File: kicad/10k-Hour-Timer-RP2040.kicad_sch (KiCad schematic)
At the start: 9 parts, among them J1 USB_C_Receptacle_USB2.0_16P, J2 JST_SH_SM03B, U1 USBLC6-2SC6

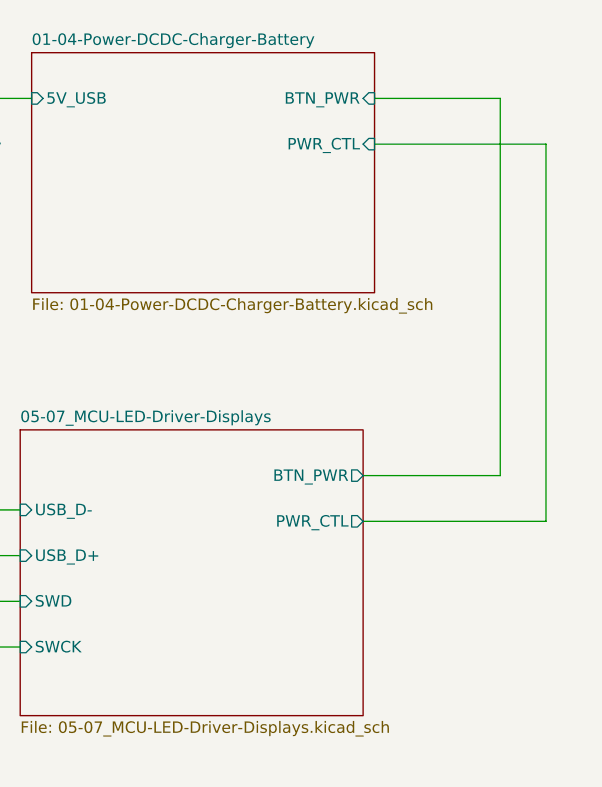
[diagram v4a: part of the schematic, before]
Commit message: rp2040 chip start
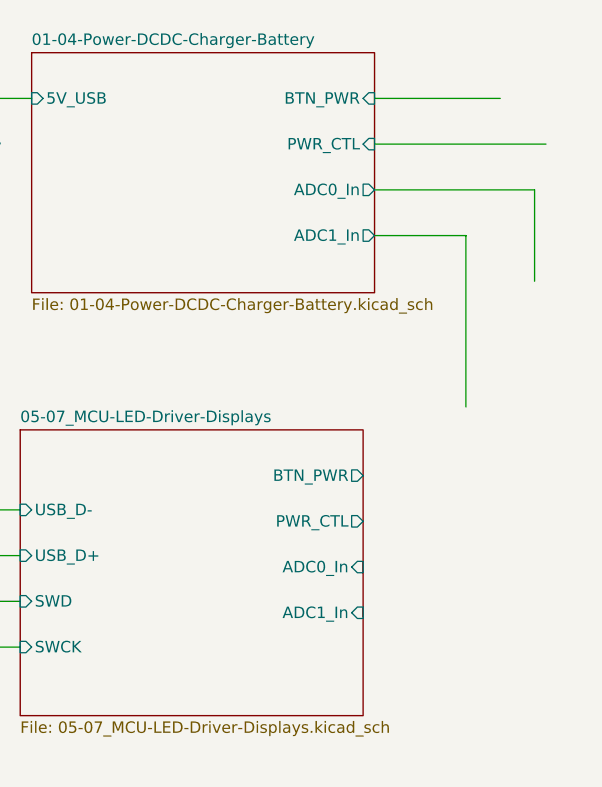
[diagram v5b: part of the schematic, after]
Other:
- sheet 01-04-Power-DCDC-Charger-Battery ports: added ADC0_In, ADC1_In; removed none
- sheet 05-07_MCU-LED-Driver-Displays ports: added ADC0_In, ADC1_In; removed none
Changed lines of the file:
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@@
-	(wire
-		(pts
-			(xy 186.69 99.06) (xy 186.69 57.15)
-		)
-		(stroke
-			(width 0)
-			(type default)
-		)
-	)
-	(wire
-		(pts
-			(xy 191.77 104.14) (xy 171.45 104.14)
-		)
-		(stroke
-			(width 0)
-			(type default)
-		)
-	)
 	(wire
 		(pts
@@
 	(wire
 		(pts
+			(xy 172.72 67.31) (xy 190.5 67.31)
+		)
+		(stroke
+			(width 0)
+			(type default)
+		)
+	)
+	(wire
+		(pts
 			(xy 57.15 123.19) (xy 60.96 123.19)
 		)
@@
 	(wire
 		(pts
-			(xy 191.77 62.23) (xy 191.77 104.14)
-		)
-		(stroke
-			(width 0)
-			(type default)
-		)
-	)
-	(wire
-		(pts
 			(xy 102.87 81.28) (xy 102.87 83.82)
 		)
@@
 	(wire
 		(pts
-			(xy 171.45 99.06) (xy 186.69 99.06)
+			(xy 172.72 72.39) (xy 182.88 72.39)
 		)
 		(stroke
@@
 	(wire
 		(pts
+			(xy 182.88 72.39) (xy 182.88 91.44)
+		)
+		(stroke
+			(width 0)
+			(type default)
+		)
+	)
+	(wire
+		(pts
 			(xy 57.15 120.65) (xy 78.74 120.65)
 		)
@@
 		(pts
 			(xy 73.66 73.66) (xy 73.66 72.39)
+		)
+		(stroke
+			(width 0)
+			(type default)
+		)
+	)
+	(wire
+		(pts
+			(xy 190.5 67.31) (xy 190.5 77.47)
 		)
 		(stroke
@@
 			)
 		)
+		(pin "ADC0_In" input
+			(at 171.45 109.22 0)
+			(effects
+				(font
+					(size 1.27 1.27)
+				)
+				(justify right)
+			)
+		)
+		(pin "ADC1_In" input
+			(at 171.45 114.3 0)
+			(effects
+				(font
+					(size 1.27 1.27)
+				)
+				(justify right)
+			)
+		)
 		(instances
 			(project "10k-Hour-Timer-RP2040"
@@
 			(effects
 				(font
+					(size 1.27 1.27)
+				)
+				(justify right)
+			)
+		)
+		(pin "ADC1_In" output
+			(at 172.72 72.39 0)
+			(effects
+				(font
+					(size 1.27 1.27)
+				)
+				(justify right)
+			)
+		)
+		(pin "ADC0_In" output
+			(at 172.72 67.31 0)
+			(effects
+				(font

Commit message: mcu periphs
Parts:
- renumbered C2 to C1, C1 to C2, J2 to J1, J1 to J2
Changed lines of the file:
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@@
 		(on_board yes)
 		(dnp no)
-		(property "Reference" "J2"
+		(property "Reference" "J1"
 			(at 49.53 122.2755 0)
 			(effects
@@
 			(project ""
 				(path "/9d26b66f-2a94-42e5-8460-016e0bf95186"
-					(reference "J2")
+					(reference "J1")
 					(unit 1)
 				)
@@
 		(on_board yes)
 		(dnp no)
-		(property "Reference" "#PWR02"
+		(property "Reference" "#PWR03"
 			(at 67.31 123.19 0)
 			(effects
@@
 			(project ""
 				(path "/9d26b66f-2a94-42e5-8460-016e0bf95186"
-					(reference "#PWR02")
+					(reference "#PWR03")
 					(unit 1)
 				)
@@
 		(on_board yes)
 		(dnp no)
-		(property "Reference" "C2"
+		(property "Reference" "C1"
 			(at 112.014 59.944 0)
 			(effects
@@
 			(project "10k-Hour-Timer-RP2040"
 				(path "/9d26b66f-2a94-42e5-8460-016e0bf95186"
-					(reference "C2")
+					(reference "C1")
 					(unit 1)
 				)
@@
 		(on_board yes)
 		(dnp no)
-		(property "Reference" "#PWR06"
+		(property "Reference" "#PWR05"
 			(at 102.87 90.17 0)
 			(effects
@@
 			(project "10k-Hour-Timer-RP2040"
 				(path "/9d26b66f-2a94-42e5-8460-016e0bf95186"
-					(reference "#PWR06")
+					(reference "#PWR05")
 					(unit 1)
 				)
@@
 		(on_board yes)
 		(dnp no)
-		(property "Reference" "#PWR013"
+		(property "Reference" "#PWR07"
 			(at 125.73 71.12 0)
 			(effects
@@
 			(project "10k-Hour-Timer-RP2040"
 				(path "/9d26b66f-2a94-42e5-8460-016e0bf95186"
-					(reference "#PWR013")
+					(reference "#PWR07")
 					(unit 1)
 				)
@@
 		(on_board yes)
 		(dnp no)
-		(property "Reference" "#PWR014"
+		(property "Reference" "#PWR01"
 			(at 52.07 137.16 0)
 			(effects
@@
 			(project "10k-Hour-Timer-RP2040"
 				(path "/9d26b66f-2a94-42e5-8460-016e0bf95186"
-					(reference "#PWR014")
+					(reference "#PWR01")
 					(unit 1)
 				)
@@
 		(dnp no)
 		(fields_autoplaced yes)
-		(property "Reference" "J1"
+		(property "Reference" "J2"
 			(at 58.42 49.53 0)
 			(effects
@@
 			(project "10k-Hour-Timer-RP2040"
 				(path "/9d26b66f-2a94-42e5-8460-016e0bf95186"
-					(reference "J1")
+					(reference "J2")
 					(unit 1)
 				)
@@
 		(on_board yes)
 		(dnp no)
-		(property "Reference" "#PWR03"
+		(property "Reference" "#PWR04"
 			(at 92.71 71.12 0)
 			(effects
@@
 			(project ""
 				(path "/9d26b66f-2a94-42e5-8460-016e0bf95186"
-					(reference "#PWR03")
+					(reference "#PWR04")
 					(unit 1)
 				)
@@
 		(on_board yes)
 		(dnp no)
-		(property "Reference" "C1"
+		(property "Reference" "C2"
 			(at 128.27 59.944 0)
 			(effects
@@
 			(project "10k-Hour-Timer-RP2040"
 				(path "/9d26b66f-2a94-42e5-8460-016e0bf95186"
-					(reference "C1")
+					(reference "C2")
 					(unit 1)
 				)
@@
 		(on_board yes)
 		(dnp no)
-		(property "Reference" "#PWR07"
+		(property "Reference" "#PWR06"
 			(at 109.22 71.12 0)
 			(effects
@@
 			(project "10k-Hour-Timer-RP2040"
 				(path "/9d26b66f-2a94-42e5-8460-016e0bf95186"
-					(reference "#PWR07")
+					(reference "#PWR06")
 					(unit 1)
 				)
@@
 		(on_board yes)
 		(dnp no)
-		(property "Reference" "#PWR05"
+		(property "Reference" "#PWR02"
 			(at 58.42 104.14 0)
 			(effects
@@
 			(project "10k-Hour-Timer-RP2040"
 				(path "/9d26b66f-2a94-42e5-8460-016e0bf95186"
-					(reference "#PWR05")
-					(unit 1)
-				)
+					(reference "#PWR02")
+					(unit 1)
+				)

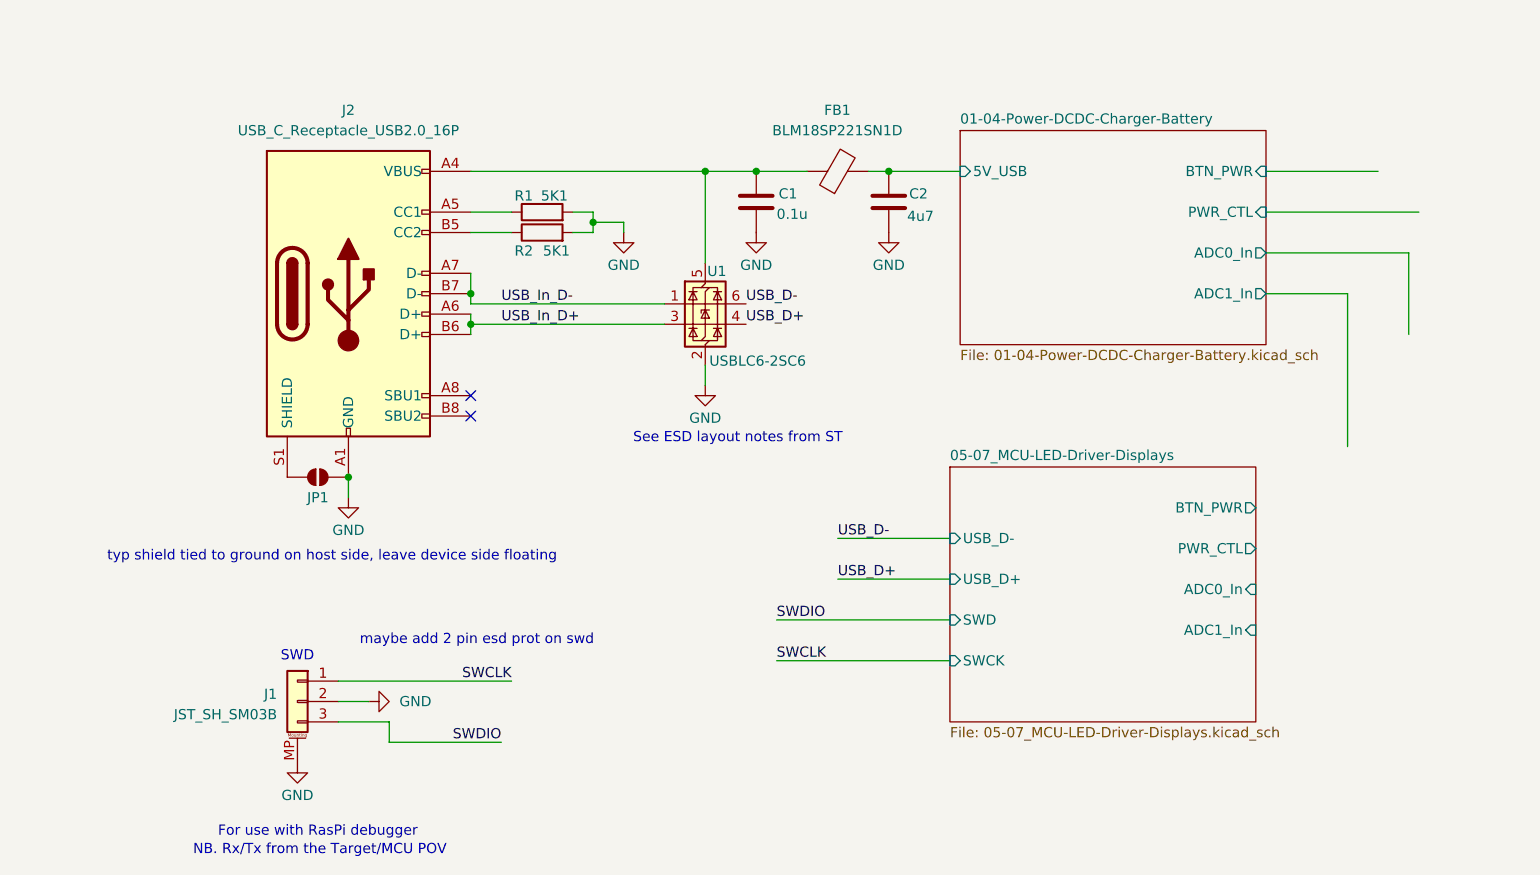
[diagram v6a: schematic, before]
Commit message: low speed xtal added
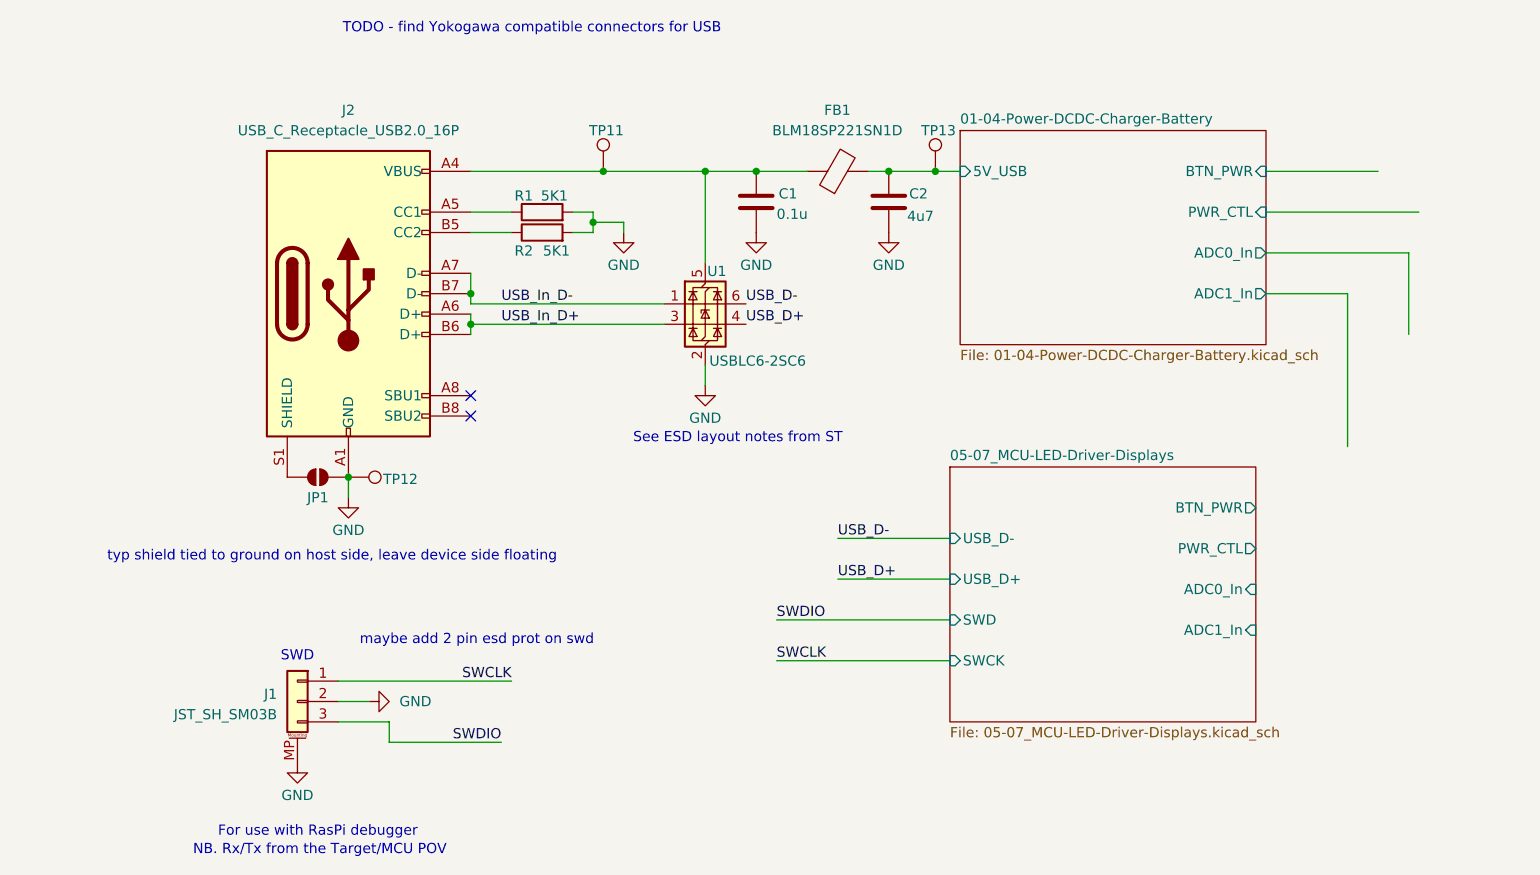
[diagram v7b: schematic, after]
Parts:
- added TP11, TP12, TP13: TestPoint, symbol Connector:TestPoint
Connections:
- net 01-04-Power-DCDC-Charger-Battery/5V_USB: now also TP13.1
- net GND: now also TP12.1
- net at C1.1, FB1.1, J2.A4 (VBUS)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: now also TP11.1
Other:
- note added: "TODO - find Yokogawa compatible connectors for USB"
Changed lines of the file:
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@@
+		)
+	)
+	(text "TODO - find Yokogawa compatible connectors for USB "
+		(exclude_from_sim no)
+		(at 81.28 39.37 0)
+		(effects
+			(font
+				(size 1.27 1.27)
+			)
 		)
 	)
@@
 	)
 	(junction
+		(at 131.5369 57.15)
+		(diameter 0)
+		(color 0 0 0 0)
+	)
+	(junction
+		(at 90.17 57.15)
+		(diameter 0)
+		(color 0 0 0 0)
+	)
+	(junction
 		(at 125.73 57.15)
 		(diameter 0)
@@
 	(wire
 		(pts
-			(xy 125.73 57.15) (xy 134.62 57.15)
+			(xy 125.73 57.15) (xy 131.5369 57.15)
 		)
 		(stroke
@@
 	(wire
 		(pts
-			(xy 73.66 57.15) (xy 102.87 57.15)
+			(xy 73.66 57.15) (xy 90.17 57.15)
 		)
 		(stroke
@@
 	(wire
 		(pts
+			(xy 90.17 57.15) (xy 102.87 57.15)
+		)
+		(stroke
+			(width 0)
+			(type default)
+		)
+	)
+	(wire
+		(pts
 			(xy 73.66 73.66) (xy 97.79 73.66)
+		)
+		(stroke
+			(width 0)
+			(type default)
+		)
+	)
+	(wire
+		(pts
+			(xy 131.5369 57.15) (xy 134.62 57.15)
 		)
 		(stroke
@@
 					(unit 1)
 				)
+			)
+		)
+	)
+	(symbol
+		(lib_id "Connector:TestPoint")
+		(at 131.5369 57.15 0)
+		(unit 1)
+		(exclude_from_sim no)
+		(in_bom yes)
+		(on_board yes)
+		(dnp no)
+		(property "Reference" "TP13"
+			(at 129.7589 52.07 0)
+			(effects
+				(font
+					(size 1.27 1.27)
+				)
+				(justify left)
+			)
+		)
+		(property "Value" "TestPoint"
+			(at 130.267 52.07 90)
+			(effects
+				(font
+					(size 1.27 1.27)
+				)
+				(justify left)
+				(hide yes)
+			)
+		)
+		(property "Footprint" ""
+			(at 136.6169 57.15 0)
+			(effects
+				(font
+					(size 1.27 1.27)
+				)
+				(hide yes)
+			)
+		)
+		(property "Datasheet" "~"
+			(at 136.6169 57.15 0)
+			(effects
+				(font
+					(size 1.27 1.27)
+				)
+				(hide yes)
+			)
+		)
+		(property "Description" "test point"
+			(at 131.5369 57.15 0)
+			(effects
+				(font
+					(size 1.27 1.27)
+				)
+				(hide yes)
+			)
+		)
+		(pin "1"
+		)
+		(instances
+			(project "10k-Hour-Timer-RP2040"
+				(path "/9d26b66f-2a94-42e5-8460-016e0bf95186"
+					(reference "TP13")
+					(unit 1)
+				)
+			)
+		)
+	)
+	(symbol
+		(lib_id "Connector:TestPoint")
+		(at 58.42 95.25 270)
+		(unit 1)
+		(exclude_from_sim no)
+		(in_bom yes)
+		(on_board yes)
+		(dnp no)
+		(property "Reference" "TP12"
+			(at 62.738 95.504 90)
+			(effects
+				(font
+					(size 1.27 1.27)
+				)
+				(justify left)
+			)
+		)
+		(property "Value" "TestPoint"
+			(at 63.5 93.9801 90)
+			(effects
+				(font
+					(size 1.27 1.27)
+				)
+				(justify left)
+				(hide yes)
+			)
+		)
+		(property "Footprint" ""
+			(at 58.42 100.33 0)
+			(effects
+				(font
+					(size 1.27 1.27)
+				)
+				(hide yes)
+			)
+		)
+		(property "Datasheet" "~"
+			(at 58.42 100.33 0)
+			(effects
+				(font
+					(size 1.27 1.27)
+				)
+				(hide yes)
+			)
+		)
+		(property "Description" "test point"
+			(at 58.42 95.25 0)
+			(effects
+				(font
+					(size 1.27 1.27)
+				)
+				(hide yes)
+			)
+		)
+		(pin "1"
+		)
+		(instances
+			(project "10k-Hour-Timer-RP2040"
+				(path "/9d26b66f-2a94-42e5-8460-016e0bf95186"
+					(reference "TP12")
+					(unit 1)
+				)
+			)
+		)
+	)
+	(symbol
+		(lib_id "Connector:TestPoint")
+		(at 90.17 57.15 0)
+		(unit 1)
+		(exclude_from_sim no)
+		(in_bom yes)
+		(on_board yes)
+		(dnp no)
+		(property "Reference" "TP11"
+			(at 88.392 52.07 0)
+			(effects
+				(font
+					(size 1.27 1.27)
+				)
+				(justify left)
+			)
+		)
+		(property "Value" "TestPoint"
+			(at 88.9001 52.07 90)
+			(effects
+				(font
+					(size 1.27 1.27)
+				)
+				(justify left)
+				(hide yes)
+			)
+		)
+		(property "Footprint" ""
+			(at 95.25 57.15 0)
+			(effects
+				(font
+					(size 1.27 1.27)
+				)
+				(hide yes)
+			)
+		)
+		(property "Datasheet" "~"
+			(at 95.25 57.15 0)
+			(effects
+				(font
+					(size 1.27 1.27)
+				)
+				(hide yes)
+			)
+		)
+		(property "Description" "test point"
+			(at 90.17 57.15 0)
+			(effects
+				(font
+					(size 1.27 1.27)
+				)
+				(hide yes)
+			)
+		)
+		(pin "1"
+		)
+		(instances
+			(project "10k-Hour-Timer-RP2040"
+				(path "/9d26b66f-2a94-42e5-8460-016e0bf95186"
+					(reference "TP11")
+					(unit 1)
+				)

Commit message: rtc hardware
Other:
- sheet 01-04-Power-DCDC-Charger-Battery ports: added ADC0_VUSB_In, ADC1_VSW_In, Vbatt; removed ADC0_In, ADC1_In
- sheet 05-07_MCU-LED-Driver-Displays ports: added ADC0_VUSB_In, ADC1_VSW_In, Vbatt; removed ADC0_In, ADC1_In
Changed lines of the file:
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@@
 	(text "TODO - find Yokogawa compatible connectors for USB "
 		(exclude_from_sim no)
-		(at 81.28 39.37 0)
+		(at 60.96 45.974 0)
 		(effects
 			(font
@@
 	(wire
 		(pts
+			(xy 134.62 72.39) (xy 127 72.39)
+		)
+		(stroke
+			(width 0)
+			(type default)
+		)
+	)
+	(wire
+		(pts
+			(xy 127 97.79) (xy 133.35 97.79)
+		)
+		(stroke
+			(width 0)
+			(type default)
+		)
+	)
+	(wire
+		(pts
 			(xy 73.66 74.93) (xy 73.66 76.2)
 		)
@@
 		(pts
 			(xy 63.5 128.27) (xy 63.5 125.73)
+		)
+		(stroke
+			(width 0)
+			(type default)
+		)
+	)
+	(wire
+		(pts
+			(xy 127 72.39) (xy 127 97.79)
 		)
 		(stroke
@@
 			)
 		)
-		(pin "ADC0_In" input
+		(pin "ADC0_VUSB_In" input
 			(at 171.45 109.22 0)
 			(effects
@@
 			)
 		)
-		(pin "ADC1_In" input
+		(pin "ADC1_VSW_In" input
 			(at 171.45 114.3 0)
 			(effects
@@
 				)
 				(justify right)
+			)
+		)
+		(pin "Vbatt" input
+			(at 133.35 97.79 180)
+			(effects
+				(font
+					(size 1.27 1.27)
+				)
+				(justify left)
 			)
 		)
@@
 			)
 		)
-		(pin "ADC1_In" output
+		(pin "ADC1_VSW_In" output
 			(at 172.72 72.39 0)
 			(effects
@@
 			)
 		)
-		(pin "ADC0_In" output
+		(pin "ADC0_VUSB_In" output
 			(at 172.72 67.31 0)
 			(effects
@@
 			)
 		)
+		(pin "Vbatt" output
+			(at 134.62 72.39 180)
+			(effects
+				(font
+					(size 1.27 1.27)
+				)
+				(justify left)
+			)
+		)
